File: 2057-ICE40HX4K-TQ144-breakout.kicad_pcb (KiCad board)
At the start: 4 copper layers, 99.1 x 66 mm, 75 parts, among them J1 Conn_02x30_Odd_Even, J2 Conn_02x30_Odd_Even, J3 RaspberryPI-B+header, J4 USB4105-GF-A, J5 RaspberryPI-B+header, J6 Conn_02x08_Odd_Even, J7 Conn_02x01, J8 Micro_SD_Card_Det, U1 ICE40HX4K-TQ144, U2 AZ1117CH-3.3TRG1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

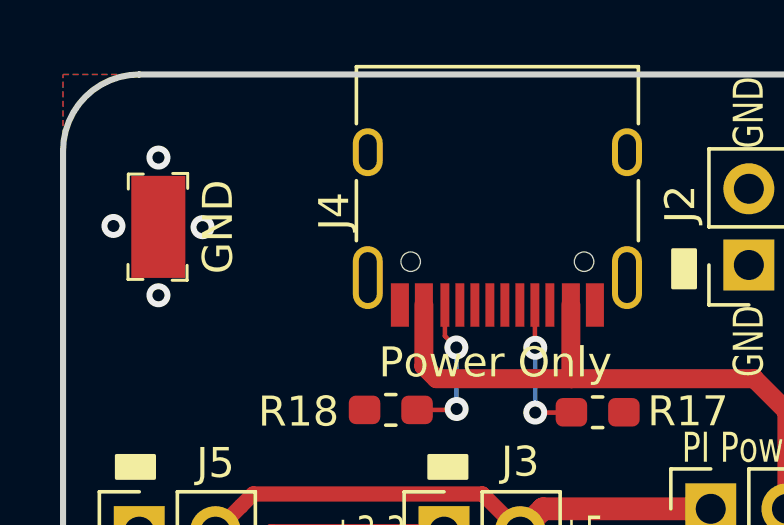
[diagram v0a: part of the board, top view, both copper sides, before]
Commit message: Fix library reference problem
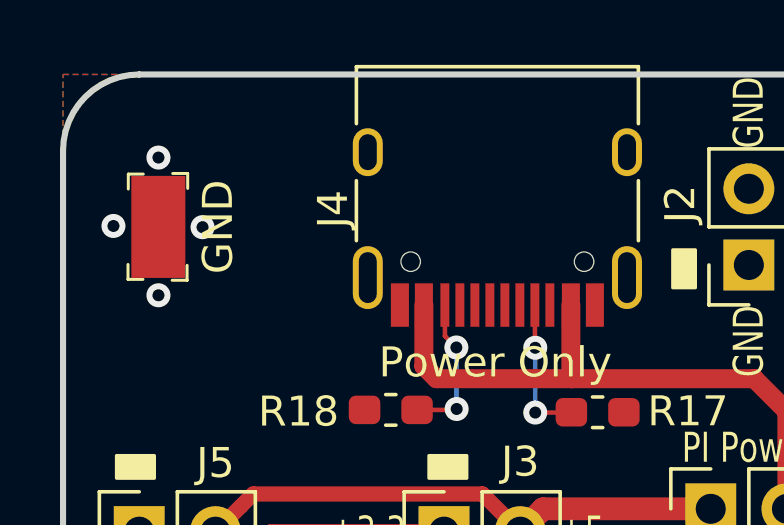
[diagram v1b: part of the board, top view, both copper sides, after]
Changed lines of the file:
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@@
     (add_net "Net-(Y1-Pad1)")
+  )
+  (module jb-footprint:USB_C_Receptacle_HRO_TYPE-C-31-M-12 (layer F.Cu)
+    (at 47.498 41.74 180)
+    (descr "USB Type-C receptacle for USB 2.0 and PD, http://www.krhro.com/uploads/soft/180320/1-1P320120243.pdf")
+    (tags "usb usb-c 2.0 pd")
+    (attr smd)
+    (fp_text reference J4 (at 5.478 -0.85 90) (layer F.SilkS)
+      (effects (font (size 1 1) (thickness 0.15)))
+    )
+    (fp_text value USB4105-GF-A (at 0 5.1) (layer F.Fab)
+      (effects (font (size 1 1) (thickness 0.15)))
+    )
+    (fp_line (start -4.7 3.9) (end 4.7 3.9) (layer F.SilkS) (width 0.12))
+    (fp_line (start -4.47 -3.65) (end 4.47 -3.65) (layer F.Fab) (width 0.1))
+    (fp_line (start -4.47 -3.65) (end -4.47 3.65) (layer F.Fab) (width 0.1))
+    (fp_line (start -4.47 3.65) (end 4.47 3.65) (layer F.Fab) (width 0.1))
+    (fp_line (start 4.47 -3.65) (end 4.47 3.65) (layer F.Fab) (width 0.1))
+    (fp_text user %R (at 0 0) (layer F.Fab)
+      (effects (font (size 1 1) (thickness 0.15)))
+    )
+    (fp_line (start -5.32 -5.27) (end 5.32 -5.27) (layer F.CrtYd) (width 0.05))
+    (fp_line (start -5.32 4.15) (end 5.32 4.15) (layer F.CrtYd) (width 0.05))
+    (fp_line (start -5.32 -5.27) (end -5.32 4.15) (layer F.CrtYd) (width 0.05))
+    (fp_line (start 5.32 -5.27) (end 5.32 4.15) (layer F.CrtYd) (width 0.05))
+    (fp_line (start 4.7 -1.9) (end 4.7 0.1) (layer F.SilkS) (width 0.12))
+    (fp_line (start 4.7 2) (end 4.7 3.9) (layer F.SilkS) (width 0.12))
+    (fp_line (start -4.7 -1.9) (end -4.7 0.1) (layer F.SilkS) (width 0.12))
+    (fp_line (start -4.7 2) (end -4.7 3.9) (layer F.SilkS) (width 0.12))
+    (pad B1 smd rect (at 3.25 -4.045 180) (size 0.6 1.45) (layers F.Cu F.Paste F.Mask)
+      (net 1 GND))
+    (pad A9 smd rect (at 2.45 -4.045 180) (size 0.6 1.45) (layers F.Cu F.Paste F.Mask)
+      (net 125 +5V))
+    (pad B9 smd rect (at -2.45 -4.045 180) (size 0.6 1.45) (layers F.Cu F.Paste F.Mask)
+      (net 125 +5V))
+    (pad B12 smd rect (at -3.25 -4.045 180) (size 0.6 1.45) (layers F.Cu F.Paste F.Mask)
+      (net 1 GND))
+    (pad A1 smd rect (at -3.25 -4.045 180) (size 0.6 1.45) (layers F.Cu F.Paste F.Mask)
+      (net 1 GND))
+    (pad A4 smd rect (at -2.45 -4.045 180) (size 0.6 1.45) (layers F.Cu F.Paste F.Mask)
+      (net 125 +5V))
+    (pad B4 smd rect (at 2.45 -4.045 180) (size 0.6 1.45) (layers F.Cu F.Paste F.Mask)
+      (net 125 +5V))
+    (pad A12 smd rect (at 3.25 -4.045 180) (size 0.6 1.45) (layers F.Cu F.Paste F.Mask)
+      (net 1 GND))
+    (pad B8 smd rect (at -1.75 -4.045 180) (size 0.3 1.45) (layers F.Cu F.Paste F.Mask)
+      (net 175 "Net-(J4-PadB8)"))
+    (pad A5 smd rect (at -1.25 -4.045 180) (size 0.3 1.45) (layers F.Cu F.Paste F.Mask)
+      (net 176 "Net-(J4-PadA5)"))
+    (pad B7 smd rect (at -0.75 -4.045 180) (size 0.3 1.45) (layers F.Cu F.Paste F.Mask)
+      (net 177 "Net-(J4-PadB7)"))
+    (pad A7 smd rect (at 0.25 -4.045 180) (size 0.3 1.45) (layers F.Cu F.Paste F.Mask)
+      (net 178 "Net-(J4-PadA7)"))
+    (pad B6 smd rect (at 0.75 -4.045 180) (size 0.3 1.45) (layers F.Cu F.Paste F.Mask)
+      (net 179 "Net-(J4-PadB6)"))
+    (pad A8 smd rect (at 1.25 -4.045 180) (size 0.3 1.45) (layers F.Cu F.Paste F.Mask)
+      (net 180 "Net-(J4-PadA8)"))
+    (pad B5 smd rect (at 1.75 -4.045 180) (size 0.3 1.45) (layers F.Cu F.Paste F.Mask)
+      (net 181 "Net-(J4-PadB5)"))
+    (pad A6 smd rect (at -0.25 -4.045 180) (size 0.3 1.45) (layers F.Cu F.Paste F.Mask)
+      (net 182 "Net-(J4-PadA6)"))
+    (pad S1 thru_hole oval (at 4.32 -3.13 180) (size 1 2.1) (drill oval 0.6 1.7) (layers *.Cu *.Mask)
+      (net 1 GND))
+    (pad S1 thru_hole oval (at -4.32 -3.13 180) (size 1 2.1) (drill oval 0.6 1.7) (layers *.Cu *.Mask)
+      (net 1 GND))
+    (pad "" np_thru_hole circle (at -2.89 -2.6 180) (size 0.65 0.65) (drill 0.65) (layers *.Cu *.Mask))
+    (pad S1 thru_hole oval (at -4.32 1.05 180) (size 1 1.6) (drill oval 0.6 1.2) (layers *.Cu *.Mask)
+      (net 1 GND))
+    (pad "" np_thru_hole circle (at 2.89 -2.6 180) (size 0.65 0.65) (drill 0.65) (layers *.Cu *.Mask))
+    (pad S1 thru_hole oval (at 4.32 1.05 180) (size 1 1.6) (drill oval 0.6 1.2) (layers *.Cu *.Mask)
+      (net 1 GND))
+    (model ${KISYS3DMOD}/Connector_USB.3dshapes/USB_C_Receptacle_HRO_TYPE-C-31-M-12.wrl
+      (at (xyz 0 0 0))
+      (scale (xyz 1 1 1))
+      (rotate (xyz 0 0 0))
+    )
   )
   (module Resistor_SMD:R_0603_1608Metric_Pad1.05x0.95mm_HandSolder (layer F.Cu)
@@
       (at (xyz 0 0 0))
       (scale (xyz 1 1 1))
-      (rotate (xyz 0 0 0))
-    )
-  )
-  (module jb-footprint:USB_C_Receptacle_HRO_TYPE-C-31-M-12 (layer F.Cu)
-    (at 47.498 41.74 180)
-    (descr "USB Type-C receptacle for USB 2.0 and PD, http://www.krhro.com/uploads/soft/180320/1-1P320120243.pdf")
-    (tags "usb usb-c 2.0 pd")
-    (attr smd)
-    (fp_text reference J4 (at 5.438 -0.92 90) (layer F.SilkS)
-      (effects (font (size 1 1) (thickness 0.15)))
-    )
-    (fp_text value USB4105-GF-A (at 0 5.1) (layer F.Fab)
-      (effects (font (size 1 1) (thickness 0.15)))
-    )
-    (fp_line (start -4.7 3.9) (end 4.7 3.9) (layer F.SilkS) (width 0.12))
-    (fp_line (start -4.47 -3.65) (end 4.47 -3.65) (layer F.Fab) (width 0.1))
-    (fp_line (start -4.47 -3.65) (end -4.47 3.65) (layer F.Fab) (width 0.1))
-    (fp_line (start -4.47 3.65) (end 4.47 3.65) (layer F.Fab) (width 0.1))
-    (fp_line (start 4.47 -3.65) (end 4.47 3.65) (layer F.Fab) (width 0.1))
-    (fp_text user %R (at 0 0) (layer F.Fab)
-      (effects (font (size 1 1) (thickness 0.15)))
-    )
-    (fp_line (start -5.32 -5.27) (end 5.32 -5.27) (layer F.CrtYd) (width 0.05))
-    (fp_line (start -5.32 4.15) (end 5.32 4.15) (layer F.CrtYd) (width 0.05))
-    (fp_line (start -5.32 -5.27) (end -5.32 4.15) (layer F.CrtYd) (width 0.05))
-    (fp_line (start 5.32 -5.27) (end 5.32 4.15) (layer F.CrtYd) (width 0.05))
-    (fp_line (start 4.7 -1.9) (end 4.7 0.1) (layer F.SilkS) (width 0.12))
-    (fp_line (start 4.7 2) (end 4.7 3.9) (layer F.SilkS) (width 0.12))
-    (fp_line (start -4.7 -1.9) (end -4.7 0.1) (layer F.SilkS) (width 0.12))
-    (fp_line (start -4.7 2) (end -4.7 3.9) (layer F.SilkS) (width 0.12))
-    (pad B1 smd rect (at 3.25 -4.045 180) (size 0.6 1.45) (layers F.Cu F.Paste F.Mask)
-      (net 1 GND))
-    (pad A9 smd rect (at 2.45 -4.045 180) (size 0.6 1.45) (layers F.Cu F.Paste F.Mask)
-      (net 125 +5V))
-    (pad B9 smd rect (at -2.45 -4.045 180) (size 0.6 1.45) (layers F.Cu F.Paste F.Mask)
-      (net 125 +5V))
-    (pad B12 smd rect (at -3.25 -4.045 180) (size 0.6 1.45) (layers F.Cu F.Paste F.Mask)
-      (net 1 GND))
-    (pad A1 smd rect (at -3.25 -4.045 180) (size 0.6 1.45) (layers F.Cu F.Paste F.Mask)
-      (net 1 GND))
-    (pad A4 smd rect (at -2.45 -4.045 180) (size 0.6 1.45) (layers F.Cu F.Paste F.Mask)
-      (net 125 +5V))
-    (pad B4 smd rect (at 2.45 -4.045 180) (size 0.6 1.45) (layers F.Cu F.Paste F.Mask)
-      (net 125 +5V))
-    (pad A12 smd rect (at 3.25 -4.045 180) (size 0.6 1.45) (layers F.Cu F.Paste F.Mask)
-      (net 1 GND))
-    (pad B8 smd rect (at -1.75 -4.045 180) (size 0.3 1.45) (layers F.Cu F.Paste F.Mask)
-      (net 175 "Net-(J4-PadB8)"))
-    (pad A5 smd rect (at -1.25 -4.045 180) (size 0.3 1.45) (layers F.Cu F.Paste F.Mask)
-      (net 176 "Net-(J4-PadA5)"))
-    (pad B7 smd rect (at -0.75 -4.045 180) (size 0.3 1.45) (layers F.Cu F.Paste F.Mask)
-      (net 177 "Net-(J4-PadB7)"))
-    (pad A7 smd rect (at 0.25 -4.045 180) (size 0.3 1.45) (layers F.Cu F.Paste F.Mask)
-      (net 178 "Net-(J4-PadA7)"))
-    (pad B6 smd rect (at 0.75 -4.045 180) (size 0.3 1.45) (layers F.Cu F.Paste F.Mask)
-      (net 179 "Net-(J4-PadB6)"))
-    (pad A8 smd rect (at 1.25 -4.045 180) (size 0.3 1.45) (layers F.Cu F.Paste F.Mask)
-      (net 180 "Net-(J4-PadA8)"))
-    (pad B5 smd rect (at 1.75 -4.045 180) (size 0.3 1.45) (layers F.Cu F.Paste F.Mask)
-      (net 181 "Net-(J4-PadB5)"))
-    (pad A6 smd rect (at -0.25 -4.045 180) (size 0.3 1.45) (layers F.Cu F.Paste F.Mask)
-      (net 182 "Net-(J4-PadA6)"))
-    (pad S1 thru_hole oval (at 4.32 -3.13 180) (size 1 2.1) (drill oval 0.6 1.7) (layers *.Cu *.Mask)
-      (net 1 GND))
-    (pad S1 thru_hole oval (at -4.32 -3.13 180) (size 1 2.1) (drill oval 0.6 1.7) (layers *.Cu *.Mask)
-      (net 1 GND))
-    (pad "" np_thru_hole circle (at -2.89 -2.6 180) (size 0.65 0.65) (drill 0.65) (layers *.Cu *.Mask))
-    (pad S1 thru_hole oval (at -4.32 1.05 180) (size 1 1.6) (drill oval 0.6 1.2) (layers *.Cu *.Mask)
-      (net 1 GND))
-    (pad "" np_thru_hole circle (at 2.89 -2.6 180) (size 0.65 0.65) (drill 0.65) (layers *.Cu *.Mask))
-    (pad S1 thru_hole oval (at 4.32 1.05 180) (size 1 1.6) (drill oval 0.6 1.2) (layers *.Cu *.Mask)
-      (net 1 GND))
-    (model ${KISYS3DMOD}/Connector_USB.3dshapes/USB_C_Receptacle_HRO_TYPE-C-31-M-12.wrl
-      (at (xyz 0 0 0))
-      (scale (xyz 1 1 1))
